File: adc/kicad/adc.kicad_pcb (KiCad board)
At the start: 2 copper layers, 90 x 88.4 mm, 106 parts, among them J1 Conn_01x02_Pin, J2 Conn_01x02_Pin, J3 Conn_01x02_Pin, J5 Conn_01x07_Pin, J6 pcie_98, U1 ADS1261BIRHBT, U2 ESD5344D-TP, U3 TPS7A2050PDBVR, U4 TPS7A2025PDBVRr, U6 TPS65135, U7 ADP7182AUJZ-5.0, U8 ADP7182AUJZ-2.5, U9 XC6206P332MR

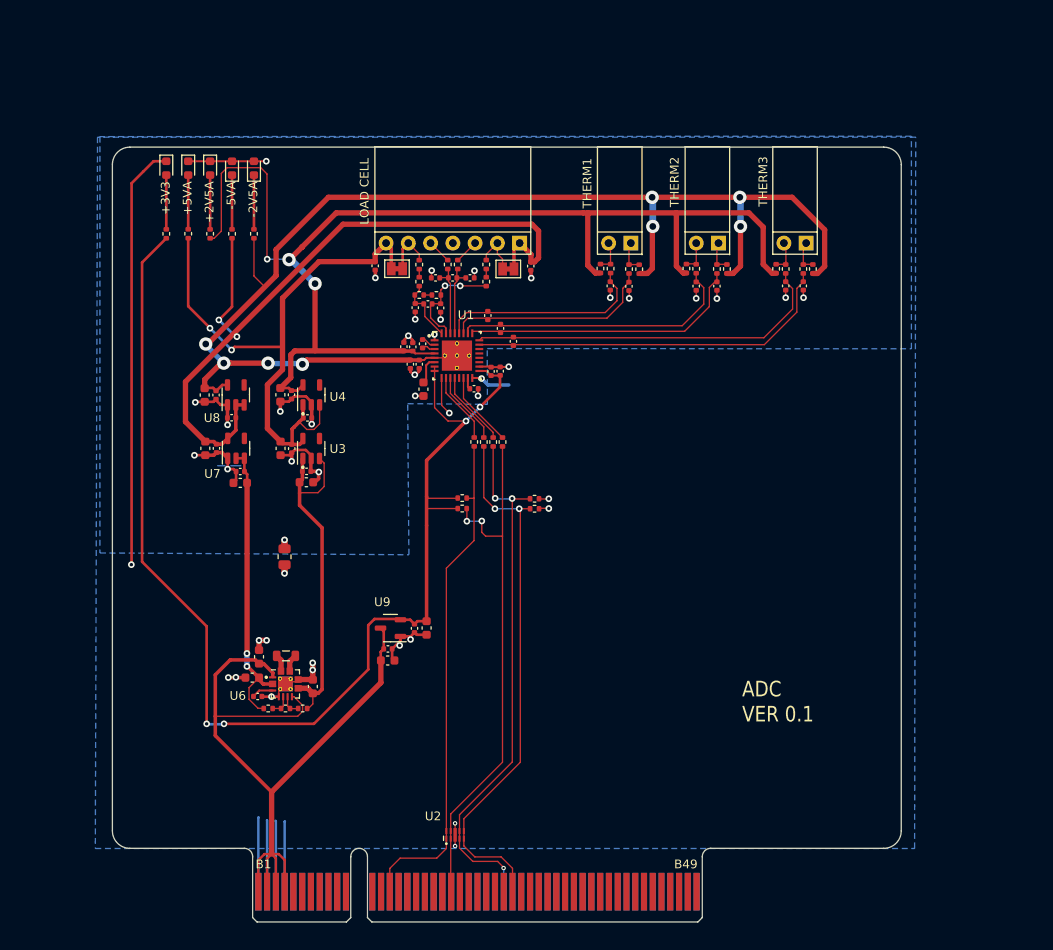
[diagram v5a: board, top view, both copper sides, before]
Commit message: More ADC layout touchups.
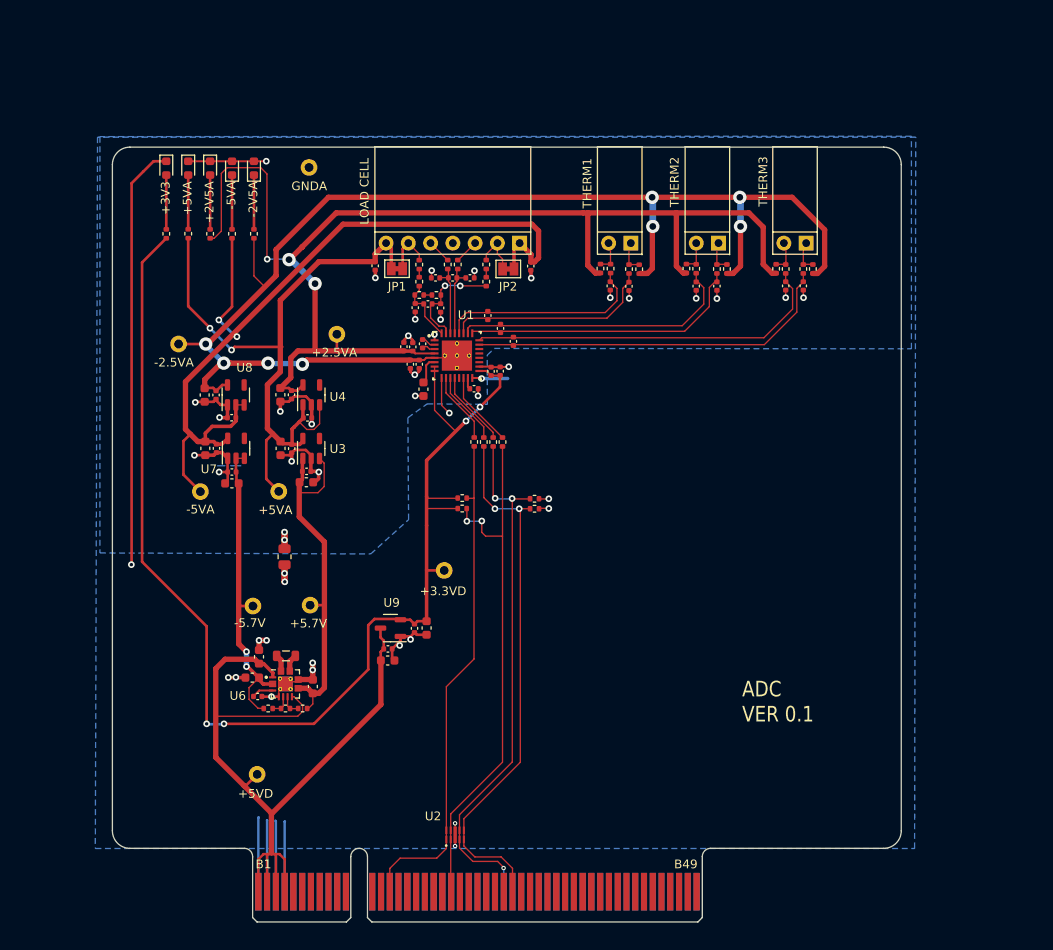
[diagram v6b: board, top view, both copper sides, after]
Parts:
- added TP1: TestPoint, common:Test_Pad, F.Cu at (-5.71, -86.1)
- added TP2: TestPoint, common:Test_Pad, F.Cu at (-11.6, -16.8)
- added TP3: TestPoint, common:Test_Pad, F.Cu at (-5.59, -36.1)
- added TP4: TestPoint, common:Test_Pad, F.Cu at (-12.1, -36.0)
- added TP5: TestPoint, common:Test_Pad, F.Cu at (-9.17, -49.1)
- added TP6: TestPoint, common:Test_Pad, F.Cu at (-18.1, -49.1)
- added TP7: TestPoint, common:Test_Pad, F.Cu at (-2.54, -67.1)
- added TP8: TestPoint, common:Test_Pad, F.Cu at (-20.6, -65.9)
- added TP9: TestPoint, common:Test_Pad, F.Cu at (9.70, -40.1)
- moved C34 0.96 mm to (-14.5, -51.3)
- moved C48 0.96 mm to (-14.5, -50.0)
- renumbered J5 to J1, J3 to J2, J1 to J3, J2 to J4, J6 to J5
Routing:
- net /-5VA: track 87.8 -> 98.7 mm
- net /+5VA: track 69.5 -> 77.0 mm
- net +5VD: track 87.9 -> 93.3 mm
- net /-2V5A: track 149.1 -> 152.2 mm
- net /-5V7: track 34.1 -> 36.3 mm
- net /+5V7: track 39.6 -> 41.4 mm
- net /+2V5A: track 140.3 -> 142.1 mm
- net /+3V3D: track 142.6 -> 144.1 mm
- net GNDA: track 60.3 -> 61.2 mm, vias 27 -> 28
- net GNDD: track 117.5 -> 118.0 mm, vias 18 -> 19
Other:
- board text added: "+2.5VA"
- board text added: "+3.3VD"
- board text added: "+5.7V"
- board text added: "+5VD"
- board text added: "-2.5VA"
- board text added: "-5.7V"
- board text added: "GNDA"
